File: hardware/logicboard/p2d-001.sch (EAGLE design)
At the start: 65 parts, among them IC1 74LS06N, IC2 4066N, IC3 MAX3468CPA, J1 MKR, J10 THS, J11 XLR, J2 GPIO, J3 Vcc, J4 RLY, J5 SPI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

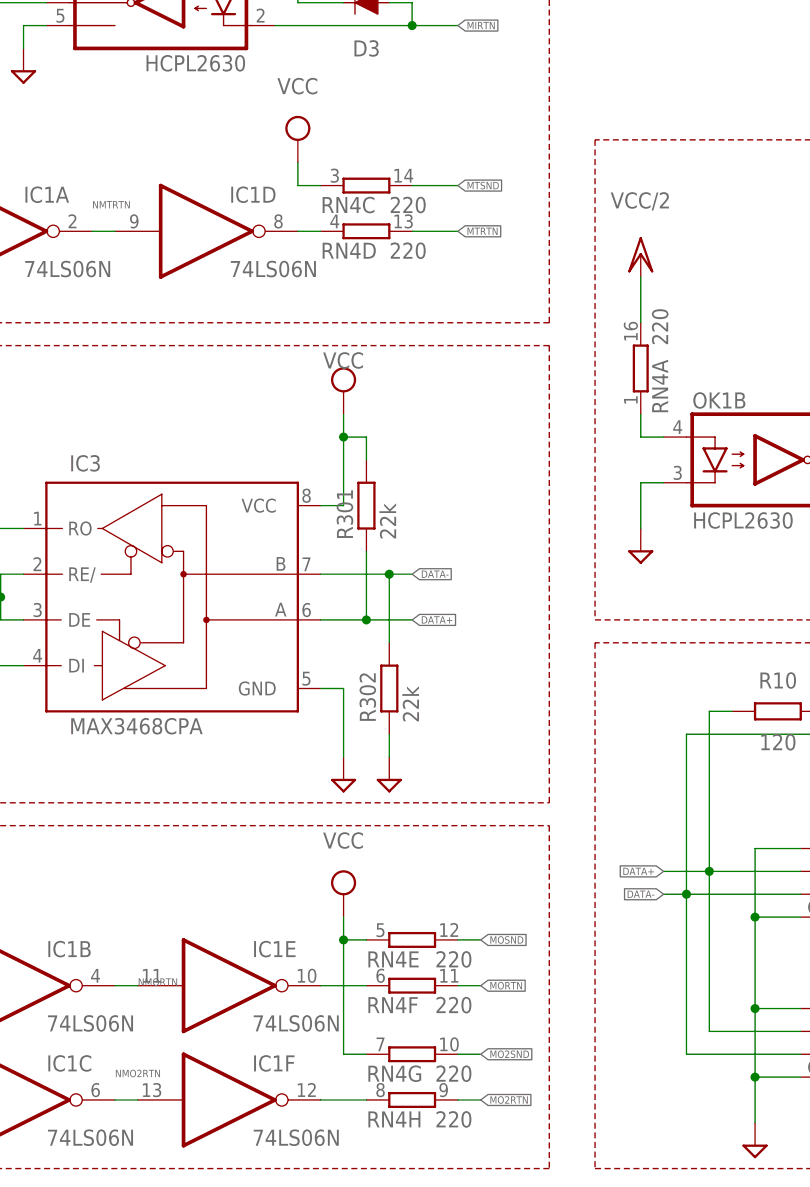
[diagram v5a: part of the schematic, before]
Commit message: Changed arrangement of R net.
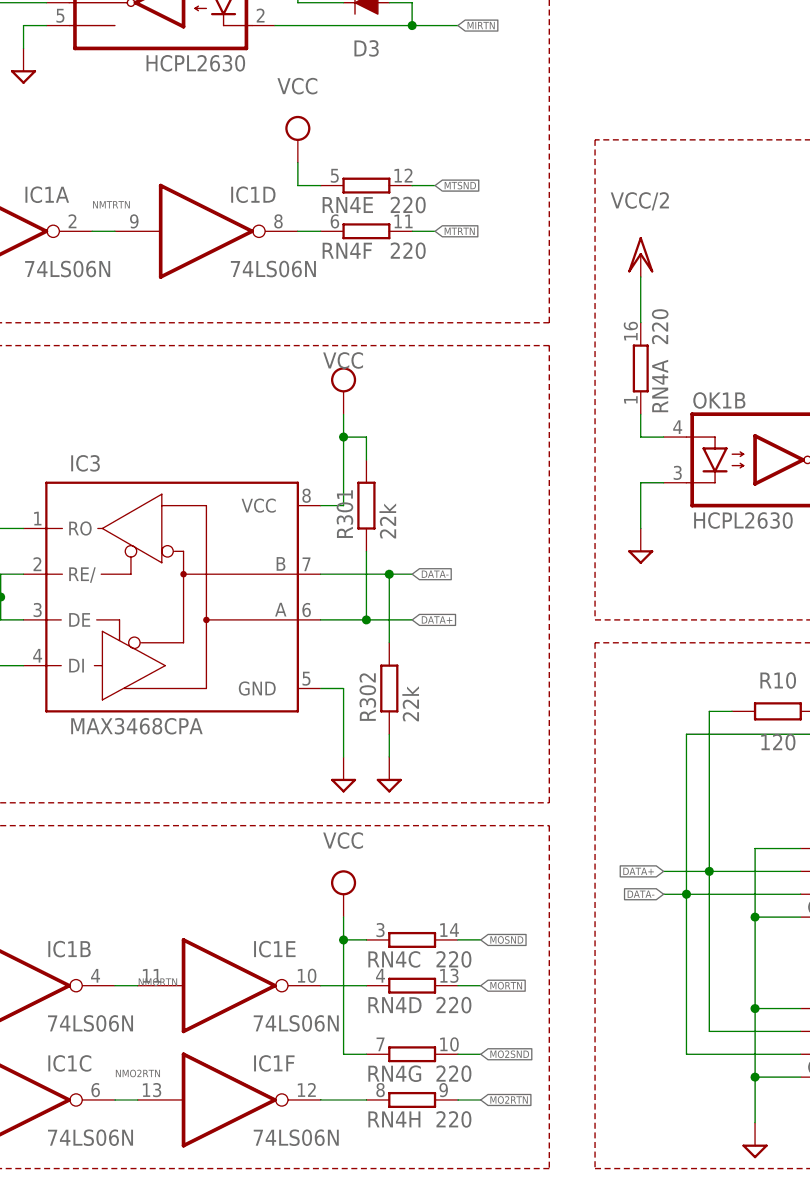
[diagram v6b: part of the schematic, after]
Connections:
- removed net N$5: IC1D.O, RN4D.1
- new net N$4: IC1E.O, RN4D.1
- net MORTN: now also RN4D.2; no longer RN4F.2
- net MOSND: now also RN4C.2; no longer RN4E.2
- net MTRTN: now also RN4F.2; no longer RN4D.2
- net MTSND: now also RN4E.2; no longer RN4C.2
- net N$3: now also IC1D.O; no longer IC1E.O
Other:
- moved on the sheet: RN4C, RN4D, RN4E, RN4F
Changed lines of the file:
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@@
 <attribute name="NAME" x="177.8" y="139.192" size="1.778" layer="95"/>
 </instance>
-<instance part="RN4" gate="C" x="182.88" y="116.84" smashed="yes">
+<instance part="RN4" gate="C" x="187.96" y="33.02" smashed="yes">
+<attribute name="VALUE" x="190.5" y="29.972" size="1.778" layer="96"/>
+<attribute name="NAME" x="182.88" y="29.972" size="1.778" layer="95"/>
+</instance>
+<instance part="RN4" gate="D" x="187.96" y="27.94" smashed="yes">
+<attribute name="VALUE" x="190.5" y="24.892" size="1.778" layer="96"/>
+<attribute name="NAME" x="182.88" y="24.892" size="1.778" layer="95"/>
+</instance>
+<instance part="RN4" gate="E" x="182.88" y="116.84" smashed="yes">
 <attribute name="VALUE" x="185.42" y="113.792" size="1.778" layer="96"/>
 <attribute name="NAME" x="177.8" y="113.792" size="1.778" layer="95"/>
 </instance>
-<instance part="RN4" gate="D" x="182.88" y="111.76" smashed="yes">
+<instance part="RN4" gate="F" x="182.88" y="111.76" smashed="yes">
 <attribute name="VALUE" x="185.42" y="108.712" size="1.778" layer="96"/>
 <attribute name="NAME" x="177.8" y="108.712" size="1.778" layer="95"/>
-</instance>
-<instance part="RN4" gate="E" x="187.96" y="33.02" smashed="yes">
-<attribute name="VALUE" x="190.5" y="29.972" size="1.778" layer="96"/>
-<attribute name="NAME" x="182.88" y="29.972" size="1.778" layer="95"/>
-</instance>
-<instance part="RN4" gate="F" x="187.96" y="27.94" smashed="yes">
-<attribute name="VALUE" x="190.5" y="24.892" size="1.778" layer="96"/>
-<attribute name="NAME" x="182.88" y="24.892" size="1.778" layer="95"/>
 </instance>
 <instance part="RN4" gate="G" x="187.96" y="20.32" smashed="yes">
@@
 <pinref part="SUPPLY17" gate="G$1" pin="VCC"/>
 <wire x1="175.26" y1="119.38" x2="175.26" y2="116.84" width="0.1524" layer="91"/>
-<pinref part="RN4" gate="C" pin="1"/>
-<wire x1="175.26" y1="116.84" x2="177.8" y2="116.84" width="0.1524" layer="91"/>
+<pinref part="RN4" gate="E" pin="1"/>
+<wire x1="177.8" y1="116.84" x2="175.26" y2="116.84" width="0.1524" layer="91"/>
 </segment>
 <segment>
 <pinref part="SUPPLY19" gate="G$1" pin="VCC"/>
 <wire x1="180.34" y1="35.56" x2="180.34" y2="33.02" width="0.1524" layer="91"/>
-<pinref part="RN4" gate="E" pin="1"/>
-<wire x1="180.34" y1="33.02" x2="182.88" y2="33.02" width="0.1524" layer="91"/>
+<pinref part="RN4" gate="C" pin="1"/>
+<wire x1="180.34" y1="33.02" x2="180.34" y2="20.32" width="0.1524" layer="91"/>
+<wire x1="182.88" y1="33.02" x2="180.34" y2="33.02" width="0.1524" layer="91"/>
+<junction x="180.34" y="33.02"/>
 <pinref part="RN4" gate="G" pin="1"/>
 <wire x1="182.88" y1="20.32" x2="180.34" y2="20.32" width="0.1524" layer="91"/>
-<wire x1="180.34" y1="33.02" x2="180.34" y2="20.32" width="0.1524" layer="91"/>
-<junction x="180.34" y="33.02"/>
 </segment>
 <segment>
@@
 </segment>
 </net>
-<net name="N$5" class="0">
-<segment>
-<pinref part="IC1" gate="D" pin="O"/>
-<pinref part="RN4" gate="D" pin="1"/>
-<wire x1="175.26" y1="111.76" x2="177.8" y2="111.76" width="0.1524" layer="91"/>
-</segment>
-</net>
-<net name="MTSND" class="0">
-<segment>
-<pinref part="RN4" gate="C" pin="2"/>
-<wire x1="187.96" y1="116.84" x2="193.04" y2="116.84" width="0.1524" layer="91"/>
-<label x="193.04" y="116.84" size="0.8128" layer="95" xref="yes"/>
-</segment>
-</net>
-<net name="MTRTN" class="0">
-<segment>
-<pinref part="RN4" gate="D" pin="2"/>
-<wire x1="187.96" y1="111.76" x2="193.04" y2="111.76" width="0.1524" layer="91"/>
-<label x="193.04" y="111.76" size="0.8128" layer="95" xref="yes"/>
-</segment>
-</net>
 <net name="DMXRX" class="0">
 <segment>
@@
 </segment>
 </net>
+<net name="MORTN" class="0">
+<segment>
+<pinref part="SV2" gate="A" pin="17"/>
+<wire x1="276.86" y1="38.1" x2="269.24" y2="38.1" width="0.1524" layer="91"/>
+<label x="269.24" y="38.1" size="0.8128" layer="95" rot="R180" xref="yes"/>
+</segment>
+<segment>
+<pinref part="RN4" gate="D" pin="2"/>
+<wire x1="193.04" y1="27.94" x2="195.58" y2="27.94" width="0.1524" layer="91"/>
+<label x="195.58" y="27.94" size="0.8128" layer="95" xref="yes"/>
+</segment>
+</net>
+<net name="MOSND" class="0">
+<segment>
+<pinref part="SV2" gate="A" pin="13"/>
+<wire x1="276.86" y1="43.18" x2="269.24" y2="43.18" width="0.1524" layer="91"/>
+<label x="269.24" y="43.18" size="0.8128" layer="95" rot="R180" xref="yes"/>
+</segment>
+<segment>
+<pinref part="RN4" gate="C" pin="2"/>
+<wire x1="193.04" y1="33.02" x2="195.58" y2="33.02" width="0.1524" layer="91"/>
+<label x="195.58" y="33.02" size="0.8128" layer="95" xref="yes"/>
+</segment>
+</net>
 <net name="N$3" class="0">
 <segment>
+<pinref part="RN4" gate="F" pin="1"/>
+<pinref part="IC1" gate="D" pin="O"/>
+<wire x1="177.8" y1="111.76" x2="175.26" y2="111.76" width="0.1524" layer="91"/>
+</segment>
+</net>
+<net name="MTSND" class="0">
+<segment>
+<pinref part="RN4" gate="E" pin="2"/>
+<wire x1="187.96" y1="116.84" x2="190.5" y2="116.84" width="0.1524" layer="91"/>
+<label x="190.5" y="116.84" size="0.8128" layer="95" xref="yes"/>
+</segment>
+</net>
+<net name="MTRTN" class="0">
+<segment>
+<pinref part="RN4" gate="F" pin="2"/>
+<wire x1="190.5" y1="111.76" x2="187.96" y2="111.76" width="0.1524" layer="91"/>
+<label x="190.5" y="111.76" size="0.8128" layer="95" xref="yes"/>
+</segment>
+</net>
+<net name="N$4" class="0">
+<segment>
+<pinref part="RN4" gate="D" pin="1"/>
 <pinref part="IC1" gate="E" pin="O"/>
-<pinref part="RN4" gate="F" pin="1"/>
-<wire x1="177.8" y1="27.94" x2="182.88" y2="27.94" width="0.1524" layer="91"/>
-</segment>
-</net>
-<net name="N$4" class="0">
-<segment>
+<wire x1="182.88" y1="27.94" x2="177.8" y2="27.94" width="0.1524" layer="91"/>
+</segment>
+</net>
+<net name="MO2SND" class="0">
+<segment>
+<pinref part="RN4" gate="G" pin="2"/>
+<wire x1="193.04" y1="20.32" x2="195.58" y2="20.32" width="0.1524" layer="91"/>
+<label x="195.58" y="20.32" size="0.8128" layer="95" xref="yes"/>
+</segment>
+</net>
+<net name="N$6" class="0">
+<segment>
+<pinref part="RN4" gate="H" pin="1"/>
 <pinref part="IC1" gate="F" pin="O"/>
-<pinref part="RN4" gate="H" pin="1"/>
-<wire x1="177.8" y1="15.24" x2="182.88" y2="15.24" width="0.1524" layer="91"/>
+<wire x1="182.88" y1="15.24" x2="177.8" y2="15.24" width="0.1524" layer="91"/>
 </segment>
 </net>
@@
 </segment>
 </net>
-<net name="MO2SND" class="0">
-<segment>
-<pinref part="RN4" gate="G" pin="2"/>
-<wire x1="193.04" y1="20.32" x2="195.58" y2="20.32" width="0.1524" layer="91"/>
-<label x="195.58" y="20.32" size="0.8128" layer="95" xref="yes"/>
-</segment>
-</net>
-<net name="MORTN" class="0">
-<segment>
-<pinref part="RN4" gate="F" pin="2"/>
-<wire x1="193.04" y1="27.94" x2="195.58" y2="27.94" width="0.1524" layer="91"/>
-<label x="195.58" y="27.94" size="0.8128" layer="95" xref="yes"/>
-</segment>
-<segment>
-<pinref part="SV2" gate="A" pin="17"/>
-<wire x1="276.86" y1="38.1" x2="269.24" y2="38.1" width="0.1524" layer="91"/>
-<label x="269.24" y="38.1" size="0.8128" layer="95" rot="R180" xref="yes"/>
-</segment>
-</net>
-<net name="MOSND" class="0">
-<segment>
-<pinref part="RN4" gate="E" pin="2"/>
-<wire x1="193.04" y1="33.02" x2="195.58" y2="33.02" width="0.1524" layer="91"/>
-<label x="195.58" y="33.02" size="0.8128" layer="95" xref="yes"/>
-</segment>
-<segment>
-<pinref part="SV2" gate="A" pin="13"/>
-<wire x1="276.86" y1="43.18" x2="269.24" y2="43.18" width="0.1524" layer="91"/>
-<label x="269.24" y="43.18" size="0.8128" layer="95" rot="R180" xref="yes"/>
-</segment>
-</net>
